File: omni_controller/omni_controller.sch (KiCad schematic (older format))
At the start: 13 parts, among them Q1 2SC1815, U1 XH_4, U2 XH_4, U3 XH_4, U4 XH_4, U5 LPC1768, U6 MPU6050, U7 R3008SB, U8 MCP2561-E-P, U9 XH_2

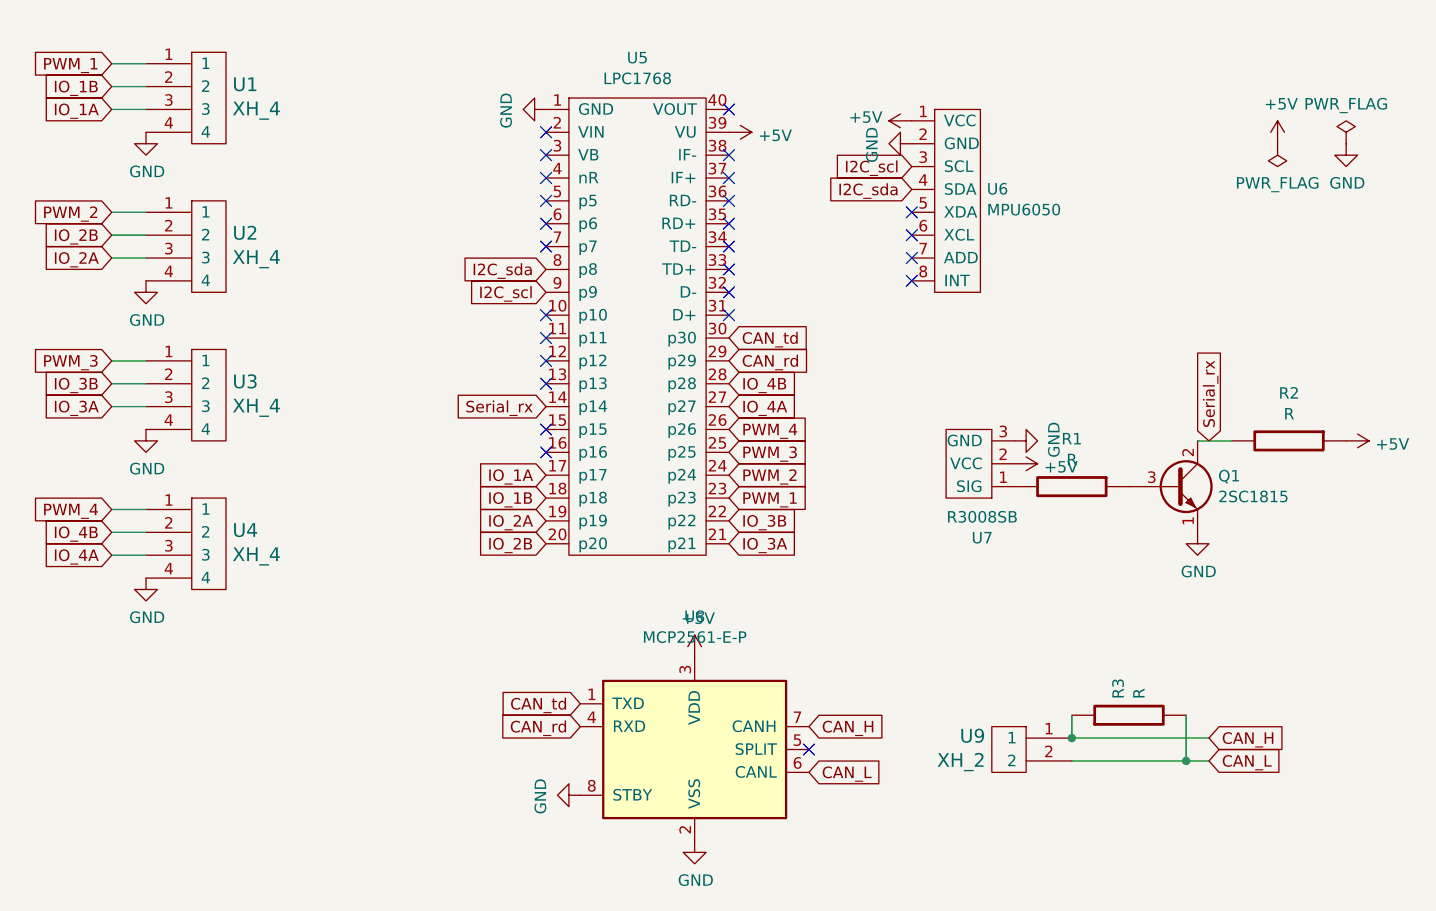
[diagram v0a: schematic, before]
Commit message: update: ライブラリの更新
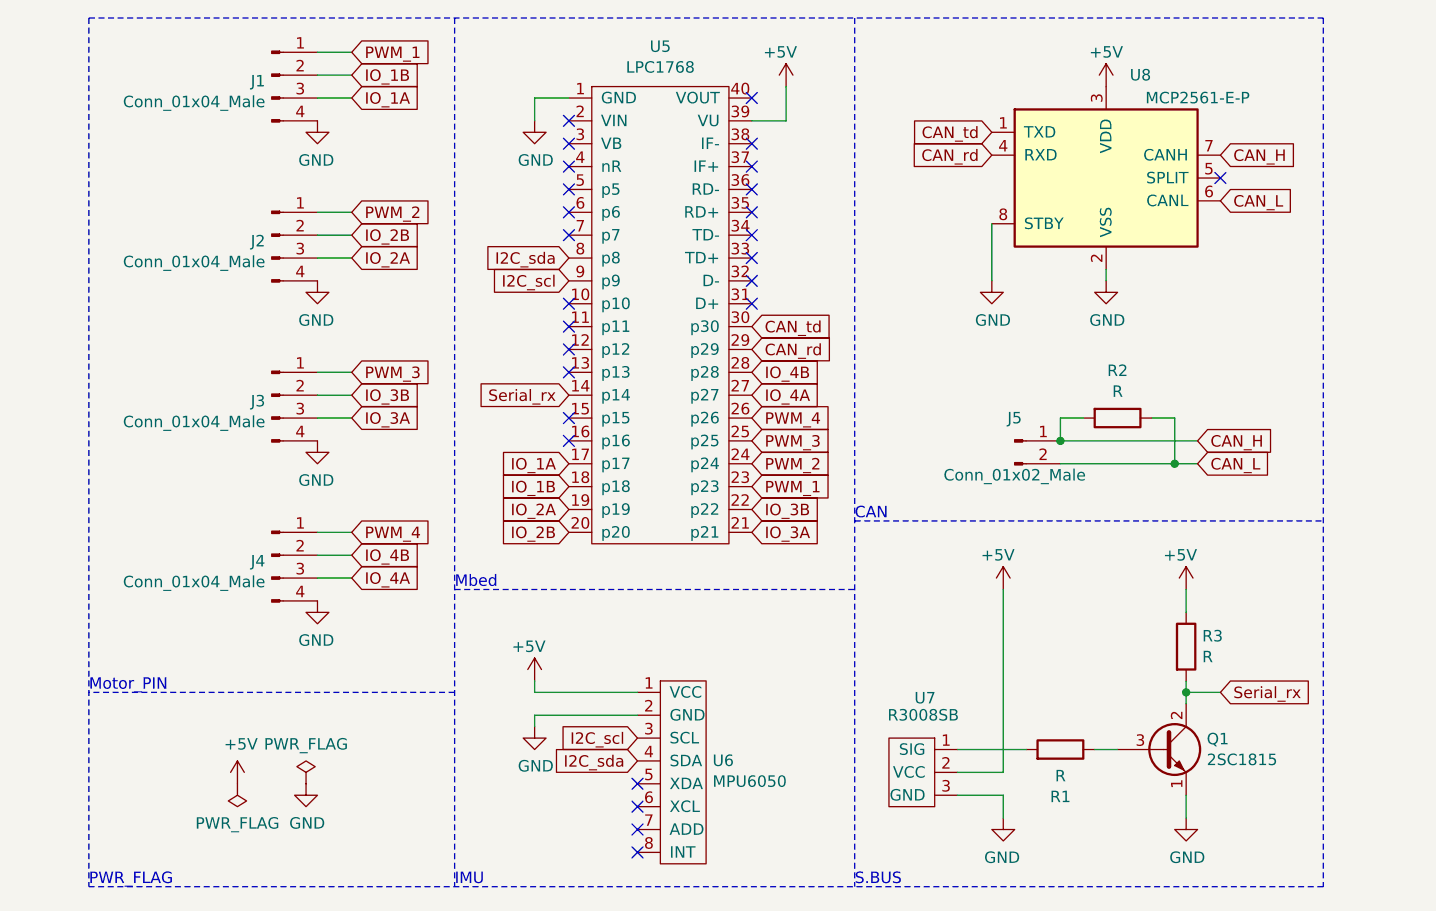
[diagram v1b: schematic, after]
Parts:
- removed R1, R2, R3: R, Resistor_THT:R_Axial_DIN0207_L6.3mm_D2.5mm_P7.62mm_Horizontal, symbol DCJACK:R
- removed U1, U2, U3, U4: XH_4, MyFootprint:JST_XH_S04B-XH-A_04x2.50mm_Angled, symbol MyComponent:XH_4
- removed U9: XH_2, MyFootprint:JST_XH_S02B-XH-A_02x2.50mm_Angled, symbol MyComponent:XH_2
- added J1, J2, J3, J4: Conn_01x04_Male, Connector_JST:JST_XH_S4B-XH-A_1x04_P2.50mm_Horizontal, symbol Connector:Conn_01x04_Male
- added J5: Conn_01x02_Male, Connector_JST:JST_XH_B2B-XH-A_1x02_P2.50mm_Vertical, symbol Connector:Conn_01x02_Male
- added R1, R2, R3: R, Resistor_THT:R_Axial_DIN0207_L6.3mm_D2.5mm_P7.62mm_Horizontal, symbol Device:R
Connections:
- net +5V: now also R3.1
- net CAN_H: now also J5.1 (Pin_1), R2.2
- net CAN_L: now also J5.2 (Pin_2), R2.1
- net GND: now also J1.4 (Pin_4), J2.4 (Pin_4), J3.4 (Pin_4), J4.4 (Pin_4)
- net IO_1A: now also J1.3 (Pin_3)
- net IO_1B: now also J1.2 (Pin_2)
- net IO_2A: now also J2.3 (Pin_3)
- net IO_2B: now also J2.2 (Pin_2)
- net IO_3A: now also J3.3 (Pin_3)
- net IO_3B: now also J3.2 (Pin_2)
- net IO_4A: now also J4.3 (Pin_3)
- net IO_4B: now also J4.2 (Pin_2)
- net PWM_1: now also J1.1 (Pin_1)
- net PWM_2: now also J2.1 (Pin_1)
- net PWM_3: now also J3.1 (Pin_1)
- net PWM_4: now also J4.1 (Pin_1)
- net Serial_rx: now also R3.2
- net at U7.1 (SIG): now also R1.2
- net at Q1.3 (B): now also R1.1
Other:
- note added: "CAN"
- note added: "IMU"
- note added: "Mbed"
- note added: "Motor_PIN"
- note added: "PWR_FLAG"
- note added: "S.BUS"
- moved on the sheet: Q1, U5, U6, U7, U8
